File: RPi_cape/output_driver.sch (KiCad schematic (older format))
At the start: 18 parts, among them U8 74LVC1G08, U9 TPS1H100B

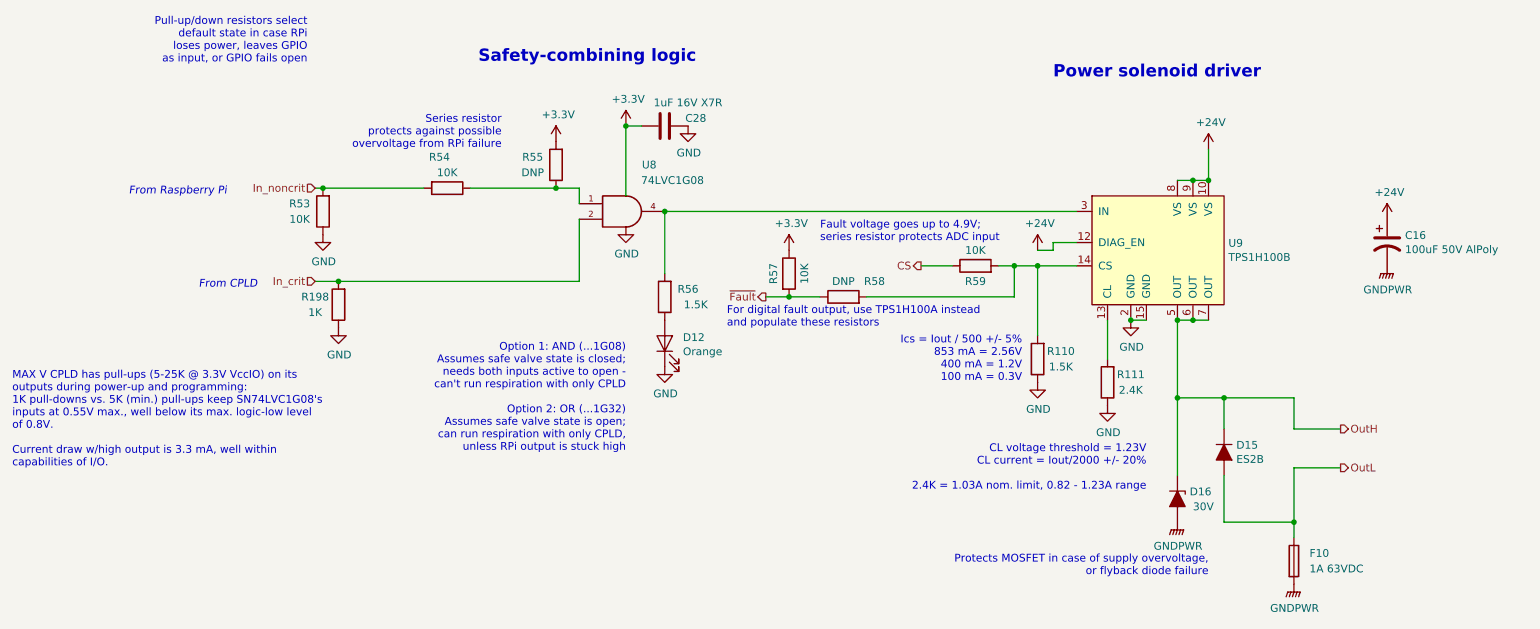
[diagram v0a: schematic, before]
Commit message: Analog upgrades and extra encoder connectors
Renamed a few files
Removed "costing BOM" as difficult to keep up to date, easy to regenerate
Toughened under-voltage detect circuits by adding hysteresis to +5V detect for +BATT diode-OR (R236), filtering to power-down alarm detect input (C85)
Added connector options (J15, J21) for Grayhill C14-series rotary encoder with cable
Changed R190 from 3K to 2.4K to increase overhead on base current required for saturation, and consolidate BOM
Added 3 solderable testpoints for expanding CPLD pin options (TP44-46), adjusted some CPLD pin assignments to allow physical routing to pins
Fixed valve motion detector by changing comparator's hysteresis to AC-only, changing NPN's series resistor to 1K (allows low-enough DC level to count as logic low), and adding optional filtering cap C115 to offset divider
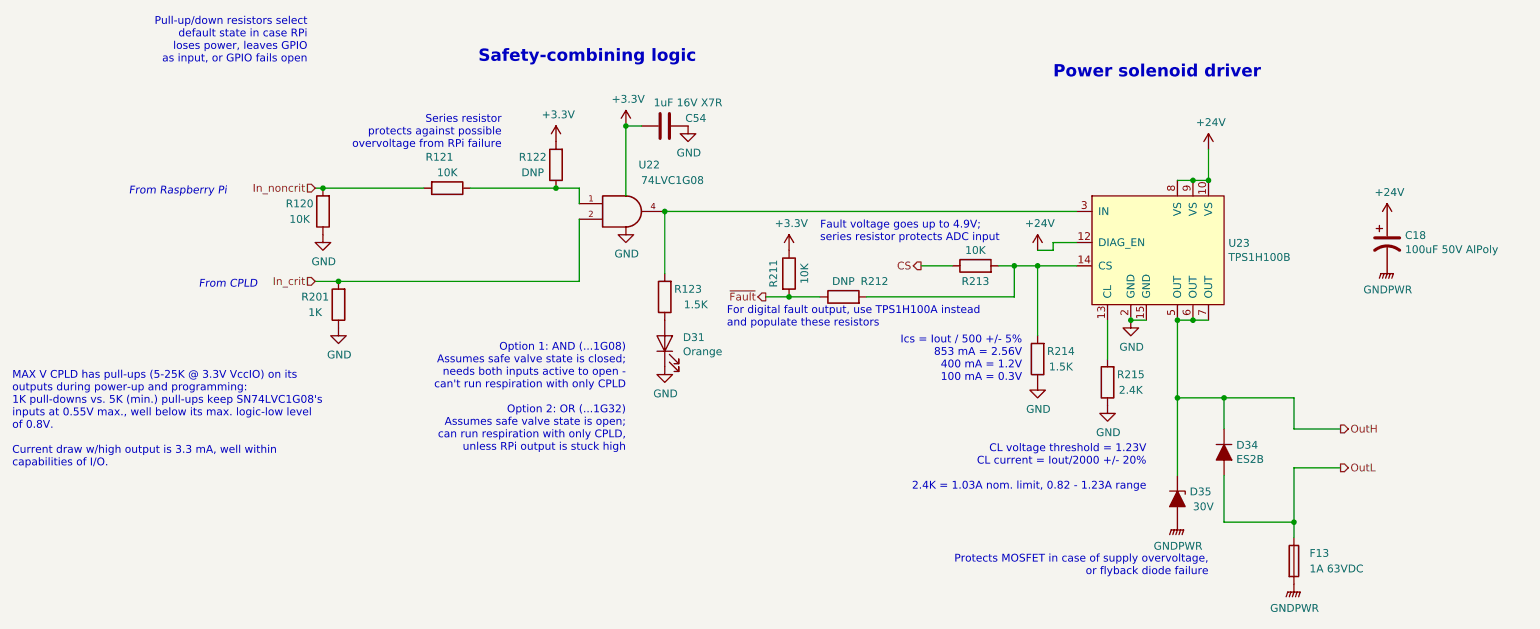
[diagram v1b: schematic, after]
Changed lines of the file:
@@
 encoding utf-8
 Sheet 3 15
-Title "Solenoid Valve Output Driver"
+Title "Raspberry Pi Hat for JamVent Adaptation"
 Date ""
-Rev "1.7"
+Rev "1.8"
 Comp "US JamVent Team"
 Comment1 "Don Straney"
@@
 AR Path="/5E8DFCAD/5E90C94B" Ref="D30"  Part="1"
 AR Path="/5E8E0754/5E90C94B" Ref="D35"  Part="1"
-F 0 "D16" V 8004 4679 50  0000 L CNN
+F 0 "D35" V 8004 4679 50  0000 L CNN
 F 1 "30V" V 8100 4700 50  0000 L CNN
 F 2 "Ventilator:D_SMA" H 8050 4600 50  0001 C CNN
@@
 AR Path="/5E8DFCAD/5E90D582" Ref="D29"  Part="1"
 AR Path="/5E8E0754/5E90D582" Ref="D34"  Part="1"
-F 0 "D15" V 8304 4379 50  0000 L CNN
+F 0 "D34" V 8304 4379 50  0000 L CNN
 F 1 "ES2B" V 8395 4379 50  0000 L CNN
 F 2 "Ventilator:D_SMA" H 8350 4300 50  0001 C CNN
@@
 AR Path="/5E8DFCAD/5E880DD0" Ref="#PWR0189"  Part="1"
 AR Path="/5E8E0754/5E880DD0" Ref="#PWR0202"  Part="1"
-F 0 "#PWR0112" H 8050 4550 50  0001 C CNN
+F 0 "#PWR0202" H 8050 4550 50  0001 C CNN
 F 1 "GNDPWR" H 8054 4596 50  0000 C CNN
 F 2 "" H 8050 4700 50  0001 C CNN
@@
 AR Path="/5E8DFCAD/5E8842DE" Ref="#PWR0187"  Part="1"
 AR Path="/5E8E0754/5E8842DE" Ref="#PWR0200"  Part="1"
-F 0 "#PWR0110" H 8250 2200 50  0001 C CNN
+F 0 "#PWR0200" H 8250 2200 50  0001 C CNN
 F 1 "+24V" H 8265 2523 50  0000 C CNN
 F 2 "" H 8250 2350 50  0001 C CNN
@@
 AR Path="/5E8DFCAD/5EA15643" Ref="U20"  Part="1"
 AR Path="/5E8DEDC0/5EA15643" Ref="U18"  Part="1"
-F 0 "U8" H 4650 3050 50  0000 C CNN
+F 0 "U22" H 4650 3050 50  0000 C CNN
 F 1 "74LVC1G08" H 4800 2950 50  0000 C CNN
 F 2 "Ventilator:SOT-23-5" H 4500 2750 50  0001 C CNN
@@
 AR Path="/5E8DFCAD/5EA17709" Ref="#PWR0180"  Part="1"
 AR Path="/5E8E0754/5EA17709" Ref="#PWR0193"  Part="1"
-F 0 "#PWR0103" H 4500 2600 50  0001 C CNN
+F 0 "#PWR0193" H 4500 2600 50  0001 C CNN
 F 1 "GND" H 4505 2677 50  0000 C CNN
 F 2 "" H 4500 2850 50  0001 C CNN
@@
 AR Path="/5E8DFCAD/5EA197B0" Ref="#PWR0179"  Part="1"
 AR Path="/5E8DEDC0/5EA197B0" Ref="#PWR0166"  Part="1"
-F 0 "#PWR0102" H 4500 2050 50  0001 C CNN
+F 0 "#PWR0192" H 4500 2050 50  0001 C CNN
 F 1 "+3.3V" H 4515 2373 50  0000 C CNN
 F 2 "" H 4500 2200 50  0001 C CNN
@@
 AR Path="/5E8DFCAD/5EA25A46" Ref="#PWR0182"  Part="1"
 AR Path="/5E8DEDC0/5EA25A46" Ref="#PWR0169"  Part="1"
-F 0 "#PWR0105" H 4900 1950 50  0001 C CNN
+F 0 "#PWR0195" H 4900 1950 50  0001 C CNN
 F 1 "GND" H 4905 2027 50  0000 C CNN
 F 2 "" H 4900 2200 50  0001 C CNN
@@
 AR Path="/5E8DFCAD/5EA25A4C" Ref="C51"  Part="1"
 AR Path="/5E8DEDC0/5EA25A4C" Ref="C48"  Part="1"
-F 0 "C28" V 4700 2400 50  0000 C CNN
+F 0 "C54" V 4700 2400 50  0000 C CNN
 F 1 "1uF 16V X7R" V 4600 2350 50  0000 C CNN
 F 2 "Capacitor_SMD:C_0805_2012Metric" H 4788 2050 50  0001 C CNN
@@
 AR Path="/5E8DFCAD/5EAB3FCE" Ref="R113"  Part="1"
 AR Path="/5E8E0754/5EAB3FCE" Ref="R120"  Part="1"
-F 0 "R53" H 2700 2700 50  0000 C CNN
+F 0 "R120" H 2700 2700 50  0000 C CNN
 F 1 "10K" H 2700 2800 50  0000 C CNN
 F 2 "Resistor_SMD:R_1206_3216Metric" V 2480 2750 50  0001 C CNN
@@
 AR Path="/5E8DFCAD/5EAB68F6" Ref="#PWR0177"  Part="1"
 AR Path="/5E8E0754/5EAB68F6" Ref="#PWR0190"  Part="1"
-F 0 "#PWR0100" H 2550 2650 50  0001 C CNN
+F 0 "#PWR0190" H 2550 2650 50  0001 C CNN
 F 1 "GND" H 2555 2727 50  0000 C CNN
 F 2 "" H 2550 2900 50  0001 C CNN
@@
 AR Path="/5E8DFCAD/5EB47B74" Ref="R115"  Part="1"
 AR Path="/5E8E0754/5EB47B74" Ref="R122"  Part="1"
-F 0 "R55" H 4200 2400 50  0000 C CNN
+F 0 "R122" H 4200 2400 50  0000 C CNN
 F 1 "DNP" H 4200 2500 50  0000 C CNN
 F 2 "Resistor_SMD:R_1206_3216Metric" V 3980 2450 50  0001 C CNN
@@
 AR Path="/5E8DFCAD/5EB49CAF" Ref="#PWR0178"  Part="1"
 AR Path="/5E8DEDC0/5EB49CAF" Ref="#PWR0165"  Part="1"
-F 0 "#PWR0101" H 4050 2150 50  0001 C CNN
+F 0 "#PWR0191" H 4050 2150 50  0001 C CNN
 F 1 "+3.3V" H 4065 2473 50  0000 C CNN
 F 2 "" H 4050 2300 50  0001 C CNN
@@
 AR Path="/5E8DFCAD/5EA292AA" Ref="R114"  Part="1"
 AR Path="/5E8E0754/5EA292AA" Ref="R121"  Part="1"
-F 0 "R54" V 3150 2550 50  0000 C CNN
+F 0 "R121" V 3150 2550 50  0000 C CNN
 F 1 "10K" V 3250 2600 50  0000 C CNN
 F 2 "Resistor_SMD:R_1206_3216Metric" V 3280 2600 50  0001 C CNN
@@
 AR Path="/5E8DFCAD/5F8B2D08" Ref="D26"  Part="1"
 AR Path="/5E8E0754/5F8B2D08" Ref="D31"  Part="1"
-F 0 "D12" V 4789 3483 50  0000 R CNN
+F 0 "D31" V 4789 3483 50  0000 R CNN
 F 1 "Orange" V 4698 3483 50  0000 R CNN
 F 2 "Ventilator:LED_0805_2012Metric" H 4750 3600 50  0001 C CNN
@@
 AR Path="/5E8DEDC0/5F8B2D0E" Ref="#PWR0168"  Part="1"
 AR Path="/5E8C8865/5F8B2D0E" Ref="#PWR?"  Part="1"
-F 0 "#PWR0104" H 4750 3500 50  0001 C CNN
+F 0 "#PWR0194" H 4750 3500 50  0001 C CNN
 F 1 "GND" H 4755 3577 50  0000 C CNN
 F 2 "" H 4750 3750 50  0001 C CNN
@@
 AR Path="/5E8DFCAD/5F8B2D14" Ref="R116"  Part="1"
 AR Path="/5E8E0754/5F8B2D14" Ref="R123"  Part="1"
-F 0 "R56" H 4600 3250 50  0000 C CNN
+F 0 "R123" H 4600 3250 50  0000 C CNN
 F 1 "1.5K" H 4550 3350 50  0000 C CNN
 F 2 "Resistor_SMD:R_1206_3216Metric" V 4680 3300 50  0001 C CNN
@@
 AR Path="/5E8DFCAD/5FA3BD23" Ref="F12"  Part="1"
 AR Path="/5E8E0754/5FA3BD23" Ref="F13"  Part="1"
-F 0 "F10" H 8900 5050 50  0000 L CNN
+F 0 "F13" H 8900 5050 50  0000 L CNN
 F 1 "1A 63VDC" H 8900 4950 50  0000 L CNN
 F 2 "Fuse:Fuse_1206_3216Metric" V 8730 5000 50  0001 C CNN
@@
 AR Path="/5E8DFCAD/5E881F2F" Ref="#PWR0188"  Part="1"
 AR Path="/5E8E0754/5E881F2F" Ref="#PWR0201"  Part="1"
-F 0 "#PWR0111" H 8800 4950 50  0001 C CNN
+F 0 "#PWR0201" H 8800 4950 50  0001 C CNN
 F 1 "GNDPWR" H 8804 4996 50  0000 C CNN
 F 2 "" H 8800 5100 50  0001 C CNN
@@
 AR Path="/5E8DFCAD/5F439429" Ref="R200"  Part="1"
 AR Path="/5E8E0754/5F439429" Ref="R201"  Part="1"
-F 0 "R198" H 2800 3300 50  0000 C CNN
+F 0 "R201" H 2800 3300 50  0000 C CNN
 F 1 "1K" H 2800 3400 50  0000 C CNN
 F 2 "Resistor_SMD:R_1206_3216Metric" V 2580 3350 50  0001 C CNN
@@
 AR Path="/5E8DFCAD/5F439819" Ref="#PWR0279"  Part="1"
 AR Path="/5E8E0754/5F439819" Ref="#PWR0280"  Part="1"
-F 0 "#PWR0275" H 2650 3250 50  0001 C CNN
+F 0 "#PWR0280" H 2650 3250 50  0001 C CNN
 F 1 "GND" H 2655 3327 50  0000 C CNN
 F 2 "" H 2650 3500 50  0001 C CNN
@@
 AR Path="/5E8DFCAD/5F780A3D" Ref="U21"  Part="1"
 AR Path="/5E8E0754/5F780A3D" Ref="U23"  Part="1"
-F 0 "U9" H 8378 3046 50  0000 L CNN
+F 0 "U23" H 8378 3046 50  0000 L CNN
 F 1 "TPS1H100B" H 8378 2955 50  0000 L CNN
 F 2 "Ventilator:TSSOP-14-1EP_4.4x5mm_P0.65mm" H 8250 2750 50  0001 C CNN
@@
 AR Path="/5E8DEDC0/5F787EEC" Ref="#PWR0171"  Part="1"
 AR Path="/5E8C8865/5F787EEC" Ref="#PWR?"  Part="1"
-F 0 "#PWR0106" H 7750 3200 50  0001 C CNN
+F 0 "#PWR0199" H 7750 3200 50  0001 C CNN
 F 1 "GND" H 7755 3277 50  0000 C CNN
 F 2 "" H 7750 3450 50  0001 C CNN
@@
 AR Path="/5E8DFCAD/5F78F2E4" Ref="#PWR0186"  Part="1"
 AR Path="/5E8E0754/5F78F2E4" Ref="#PWR0344"  Part="1"
-F 0 "#PWR0107" H 7150 2850 50  0001 C CNN
+F 0 "#PWR0344" H 7150 2850 50  0001 C CNN
 F 1 "+24V" H 7165 3173 50  0000 C CNN
 F 2 "" H 7150 3000 50  0001 C CNN
@@
 AR Path="/5E8DFCAD/5F79579F" Ref="R210"  Part="1"
 AR Path="/5E8E0754/5F79579F" Ref="R215"  Part="1"
-F 0 "R111" H 7450 3800 50  0000 C CNN
+F 0 "R215" H 7450 3800 50  0000 C CNN
 F 1 "2.4K" H 7450 3900 50  0000 C CNN
 F 2 "Resistor_SMD:R_1206_3216Metric" V 7530 3850 50  0001 C CNN
@@
 AR Path="/5E8DEDC0/5F7964D9" Ref="#PWR0173"  Part="1"
 AR Path="/5E8C8865/5F7964D9" Ref="#PWR?"  Part="1"
-F 0 "#PWR0108" H 7600 3750 50  0001 C CNN
+F 0 "#PWR0345" H 7600 3750 50  0001 C CNN
 F 1 "GND" H 7605 3827 50  0000 C CNN
 F 2 "" H 7600 4000 50  0001 C CNN
@@
 AR Path="/5E8DFCAD/5F7975EB" Ref="R209"  Part="1"
 AR Path="/5E8E0754/5F7975EB" Ref="R214"  Part="1"
-F 0 "R110" H 7000 3650 50  0000 C CNN
+F 0 "R214" H 7000 3650 50  0000 C CNN
 F 1 "1.5K" H 7000 3750 50  0000 C CNN
 F 2 "Resistor_SMD:R_1206_3216Metric" V 7080 3700 50  0001 C CNN
@@
 AR Path="/5E8DEDC0/5F79842D" Ref="#PWR0183"  Part="1"
 AR Path="/5E8C8865/5F79842D" Ref="#PWR?"  Part="1"
-F 0 "#PWR0109" H 7150 3600 50  0001 C CNN
+F 0 "#PWR0346" H 7150 3600 50  0001 C CNN
 F 1 "GND" H 7155 3677 50  0000 C CNN
 F 2 "" H 7150 3850 50  0001 C CNN
@@
 AR Path="/5E8DFCAD/5F7A701D" Ref="R208"  Part="1"
 AR Path="/5E8E0754/5F7A701D" Ref="R213"  Part="1"
-F 0 "R59" V 6650 3100 50  0000 C CNN
+F 0 "R213" V 6650 3100 50  0000 C CNN
 F 1 "10K" V 6850 3100 50  0000 C CNN
 F 2 "Resistor_SMD:R_1206_3216Metric" V 6680 3100 50  0001 C CNN
@@
 AR Path="/5E8DFCAD/5F7C8CC4" Ref="R126"  Part="1"
 AR Path="/5E8E0754/5F7C8CC4" Ref="R212"  Part="1"
-F 0 "R58" V 6000 3100 50  0000 C CNN
+F 0 "R212" V 6000 3100 50  0000 C CNN
 F 1 "DNP" V 6000 3300 50  0000 C CNN
 F 2 "Resistor_SMD:R_1206_3216Metric" V 5830 3300 50  0001 C CNN
@@
 AR Path="/5E8DFCAD/5F7C929B" Ref="R125"  Part="1"
 AR Path="/5E8E0754/5F7C929B" Ref="R211"  Part="1"
-F 0 "R57" V 5450 3150 50  0000 C CNN
+F 0 "R211" V 5450 3150 50  0000 C CNN
 F 1 "10K" V 5650 3150 50  0000 C CNN
 F 2 "Resistor_SMD:R_1206_3216Metric" V 5480 3150 50  0001 C CNN
@@
 AR Path="/5E8DFCAD/5F7C971E" Ref="#PWR0198"  Part="1"
 AR Path="/5E8DEDC0/5F7C971E" Ref="#PWR0184"  Part="1"
-F 0 "#PWR0170" H 5550 2850 50  0001 C CNN
+F 0 "#PWR0347" H 5550 2850 50  0001 C CNN
 F 1 "+3.3V" H 5565 3173 50  0000 C CNN
 F 2 "" H 5550 3000 50  0001 C CNN
@@
 AR Path="/5E8DFCAD/5FCCF122" Ref="C17"  Part="1"
 AR Path="/5E8E0754/5FCCF122" Ref="C18"  Part="1"
-F 0 "C16" H 9515 2996 50  0000 L CNN
+F 0 "C18" H 9515 2996 50  0000 L CNN
 F 1 "100uF 50V AlPoly" H 9515 2905 50  0000 L CNN
 F 2 "Capacitor_SMD:CP_Elec_10x10.5" H 9400 2950 50  0001 C CNN
@@
 AR Path="/5E8E0754/5FCCF128" Ref="#PWR0354"  Part="1"
 AR Path="/5FCCF128" Ref="#PWR?"  Part="1"
-F 0 "#PWR0348" H 9400 2650 50  0001 C CNN
+F 0 "#PWR0354" H 9400 2650 50  0001 C CNN
 F 1 "+24V" H 9415 2973 50  0000 C CNN
 F 2 "" H 9400 2800 50  0001 C CNN
@@
 AR Path="/5E8E0754/5FCCF12E" Ref="#PWR0355"  Part="1"
 AR Path="/5FCCF12E" Ref="#PWR?"  Part="1"
-F 0 "#PWR0349" H 9400 2900 50  0001 C CNN
+F 0 "#PWR0355" H 9400 2900 50  0001 C CNN
 F 1 "GNDPWR" H 9404 2946 50  0000 C CNN
 F 2 "" H 9400 3050 50  0001 C CNN

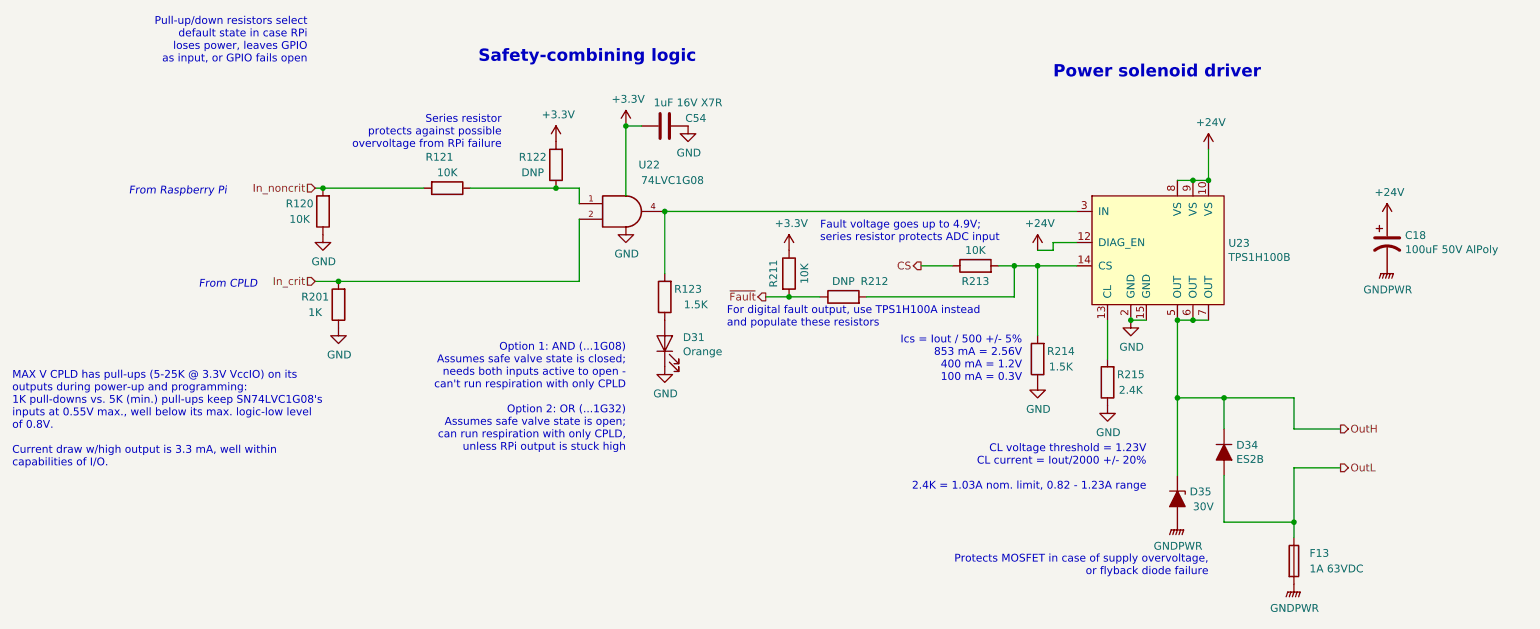
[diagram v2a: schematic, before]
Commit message: Admin (naming, license), improvements based on testing
Updated name on schematic, PCB silkscreen
Added 3 mounting holes on inside area of board for better mechanical robustness
Removed extra unused pressure sensor barb packages from library
Fixed Phoenix spring connector footprints, and added 3D models from Phoenix website
Added 3D models to TE encoder connector footprints, QFP-100 for CPLD, and 5019 testpoint
Changed DIAG_EN pin connection from valve drivers from +24V (too high) to +3.3V
Added CERN licensing terms
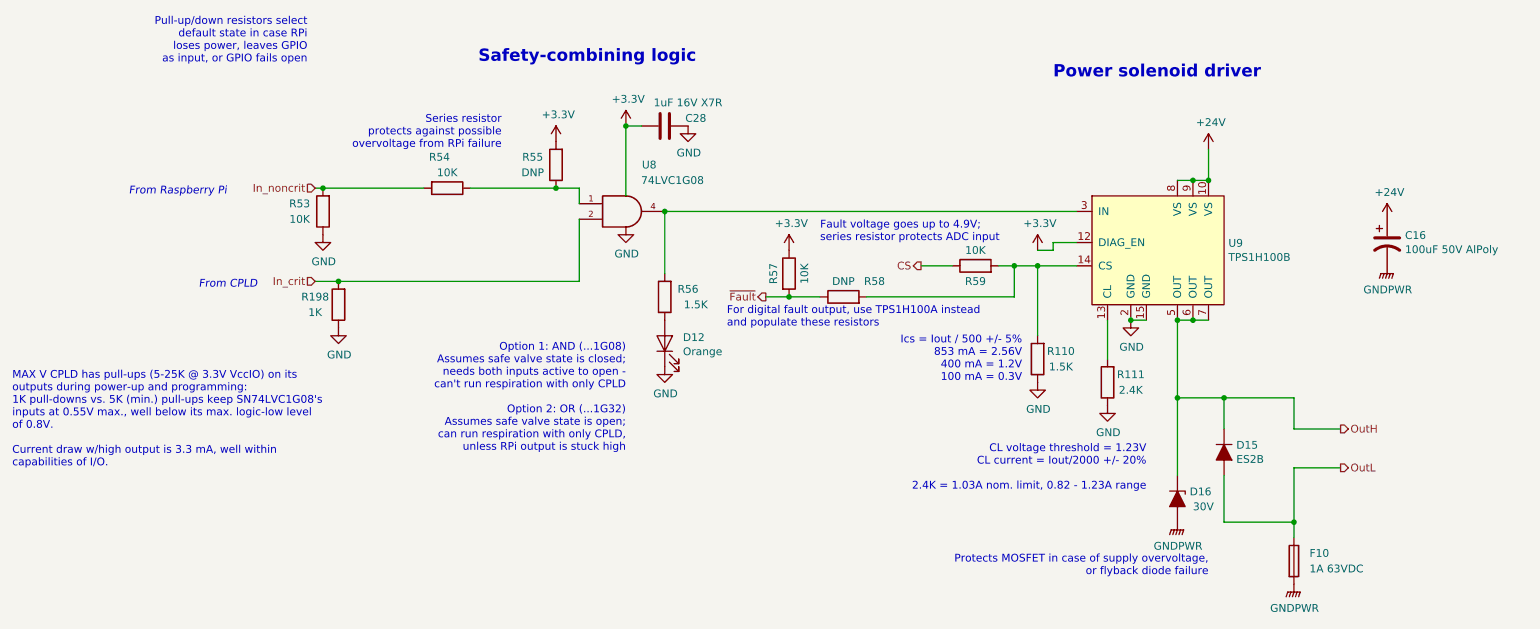
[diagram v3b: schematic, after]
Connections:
- net +24V: no longer U9.12 (DIAG_EN)
- net +3V3: now also U9.12 (DIAG_EN)
